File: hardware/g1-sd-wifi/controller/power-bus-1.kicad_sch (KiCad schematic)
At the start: 48 parts, among them J20 5V/GND direct wire pads, Q20 PMV48XP reverse polarity, U20 TPS2116 automatic mux, U21 TPS62162 3.3V 1A, U22 TPS62162 3.3V 1A, U23 TPS3808G33DBVR, U24 TPS3808G33DBVR, U25 TPS3808G33DBVR, U26 TPS3808G01DBVR, U27 SN74LVC2G08DCUR, U28 SN74LVC2G08DCUR, U29 SN74LVC2G08DCUR, U30 SN74LVC1G11DBVR

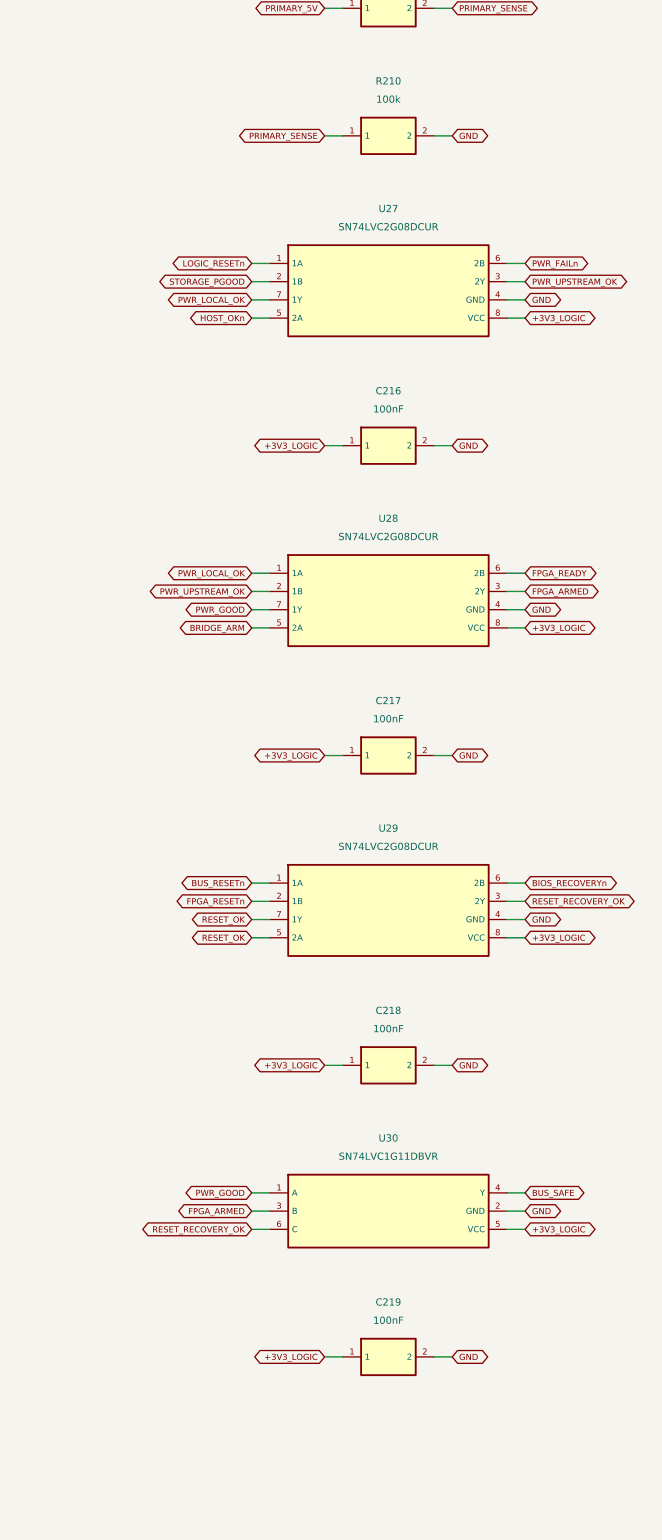
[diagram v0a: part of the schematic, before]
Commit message: G1 carrier: 1k R410, 4.18 V loss threshold, local bypass placement
- R410 becomes a 1 kOhm pull-up (reused 0402 part), so a selector harness
  fitted with R410 still present cannot short console 3.3 V.
- R270 (4.7 kOhm, reused part) lowers the U26 loss threshold from 4.358 V
  to 4.180 V; the divider now sits beside U26 instead of 27 mm away.
- 28 owner-assigned bypass capacitors placed next to their ICs with a new
  placer (tools/place_local_bypass.py); C230 and the DNP BIOS caps for
  U42/U43 remain open. C236 moves to the C5 load.
- tools/update_board_from_netlist.py applies reviewed schematic changes to
  the routed board without re-placing it.
- generate_design.py takes KICAD10_FOOTPRINT_DIR so an older system library
  cannot overwrite the localized KiCad 10 footprints.

Native ERC 0, DRC 0, parity 0; integration audit refreshed and passing.

Co-Authored-By: Claude Opus 5.5 <noreply@anthropic.com>
Claude-Session: https://claude.ai/code/session_01Gp9EYc2r9fMpZ7V8WtfonZ
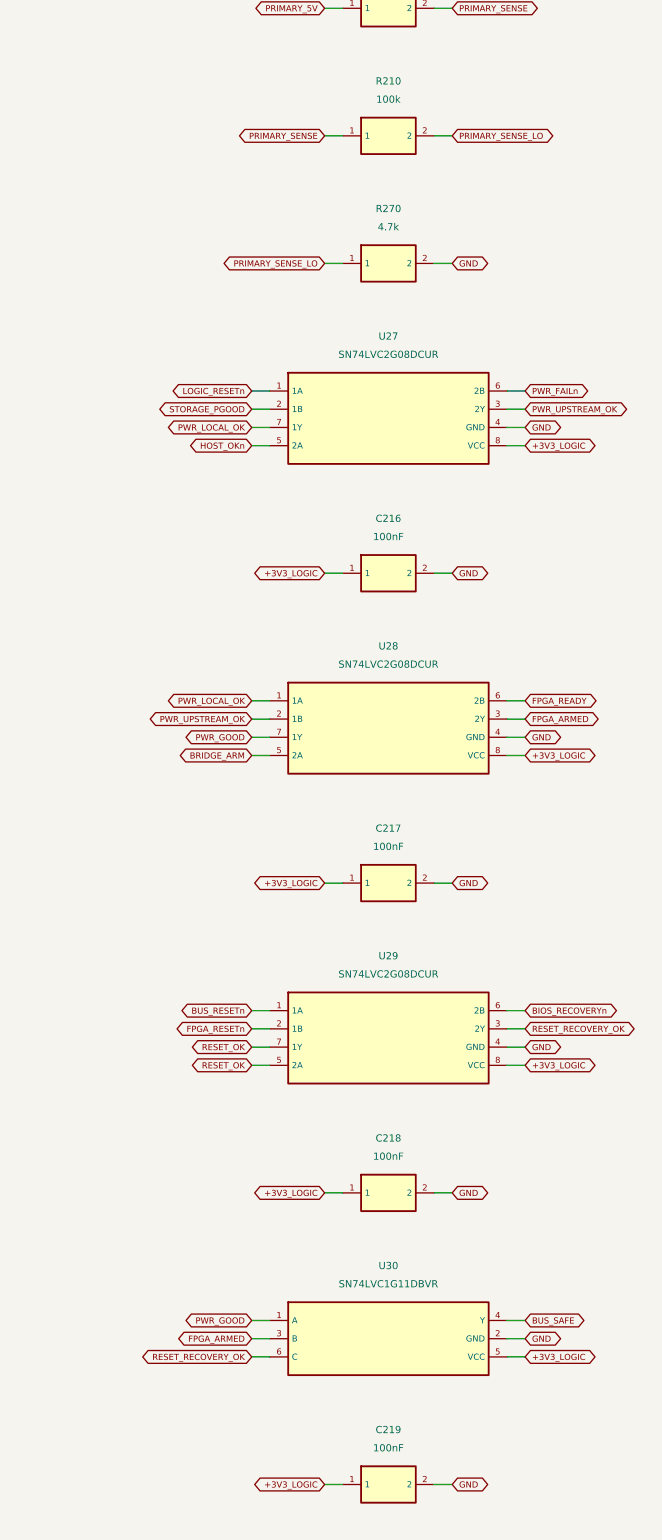
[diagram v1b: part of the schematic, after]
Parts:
- added R270: 4.7k, KUI_Footprints:R_0402_1005Metric, symbol KUI_G1:R270
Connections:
- net GND: now also R270.2; no longer R210.2
- new net PRIMARY_SENSE_LO: R210.2, R270.1
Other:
- moved on the sheet: C216, C217, C218, C219, U27, U28, U29, U30

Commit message: G1 carrier: D21 input TVS turns a 12-V mis-wire into a blown F20
A bidirectional 5-V TVS (SMF5.0CA, SOD-123FL) from FUSED_5V to GND,
between F20 and Q20: above about 6.4 V it conducts far more than F20's
1.5 A rating, so a wrong 12-V feed opens the fuse instead of sitting on
the 5-V parts. Bidirectional, so a reversed 5-V feed stays below
breakdown and Q20 blocks it without blowing F20. Downstream parts may
still see the ~9 V clamp while F20 clears; the doc says so.

Schematic, netlist, ERC (0), integration audit (361 parts) and parts
list regenerated. Its datasheet and JLC catalog identity could not be
reached from this environment, so the part is listed sourcing-pending.
The floorplan places D21 2.2 mm from F20's output; the netlist updater
can now add a part whose footprint is not on the board yet. The power
doc also notes that F20 does not protect the harness itself.

Co-Authored-By: Claude Opus 5.5 <noreply@anthropic.com>
Claude-Session: https://claude.ai/code/session_01Gp9EYc2r9fMpZ7V8WtfonZ
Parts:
- removed C219: 100nF, KUI_Footprints:C_0402_1005Metric, symbol KUI_G1:C219
- added D21: 5 V bidirectional TVS, KUI_Footprints:D_SOD-123F, symbol KUI_G1:D21
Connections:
- net FUSED_5V: now also D21.1
- net GND: now also D21.2
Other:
- moved on the sheet: C200, C201, C202, C203, C204, C205, C206, C207, C208, C209, C210, C211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

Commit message: G1 safety: fuse the host 3.3-V entry; no console 5 V on the flex or carrier
Host 3.3 V reached about 30 carrier parts straight from two flex contacts,
and the two console-5-V contacts were joined by an unused carrier trace;
a short on either would load a console supply through 0.5 A connector
contacts with no fuse anywhere. Now:

- F21 (0467.500NR, 0.5 A fast, same 467 family as F20) sits between the one
  remaining 3.3-V entry, J51 B1, and CONSOLE_3V3. If it opens the buffers
  lose VCCB and isolate, and U25 reports the host rail absent.
- CN503 A1 (second 3.3 V) and A3/B3 (5 V) get no flex copper at all: no
  landing pad, no trace, only an unconnected mating finger, so a chafed
  flex cannot short a console supply. Their carrier socket pins are bare.
  flex-interface.json lists them; the flex and carrier generators and both
  checks read that list. Flex ERC/DRC/parity 0; carrier ERC 0, integration
  check pass (362 parts).
- The DSN export keeps the 5-V and storage supply nets on the 1 oz outer
  layers: on 0.5 oz inner copper a 0.25 mm track at the fuse current would
  overheat (IPC-2221).
- F21 is placed by the floorplan next to J51; board DRC 0, parity 0
  (unrouted).

Co-Authored-By: Claude Opus 5.5 <noreply@anthropic.com>
Claude-Session: https://claude.ai/code/session_01Gp9EYc2r9fMpZ7V8WtfonZ
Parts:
- removed U30: SN74LVC1G11DBVR, KUI_Footprints:SOT-23-6, symbol KUI_G1:U30
- added F21: 0.5A fast fuse, KUI_Footprints:Fuse_0603_1608Metric, symbol KUI_G1:F21
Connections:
- net CONSOLE_3V3: now also F21.2
- new net CONSOLE_3V3_FLEX: F21.1
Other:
- moved on the sheet: C200, C201, C202, C203, C204, C205, C206, C207, C208, C209, C210, C211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
